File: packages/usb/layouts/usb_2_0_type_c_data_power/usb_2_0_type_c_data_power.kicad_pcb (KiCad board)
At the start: 2 copper layers, 5 parts

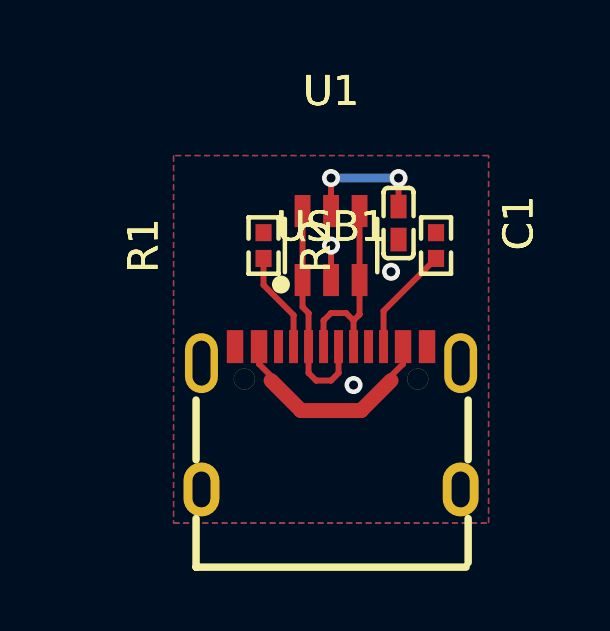
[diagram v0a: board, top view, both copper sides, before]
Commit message: Add ESP32S3, BM9002, Logic; Various naming updates and splitting of packages
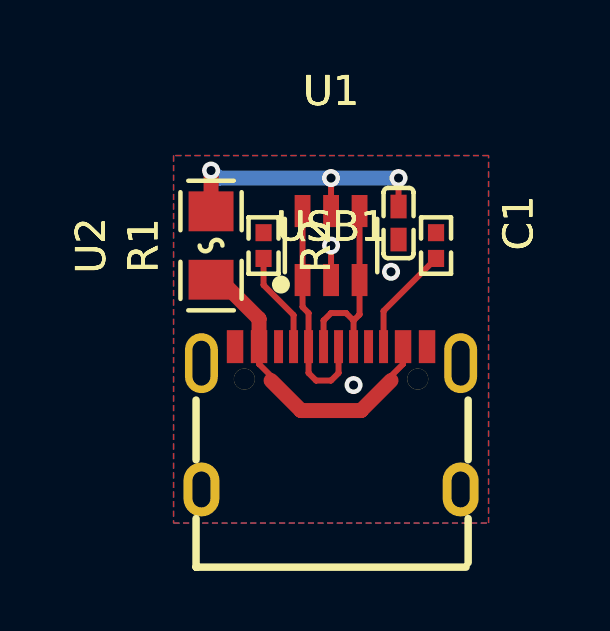
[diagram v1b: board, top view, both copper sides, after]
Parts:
- added U2: , atopile:F0805-d5954a, F.Cu at (-4.00, -5.75)
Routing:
- net hv: track 4.30 -> 9.76 mm, vias 2 -> 3
- net VBUS: track 7.42 -> 10.5 mm

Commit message: Build all packages without designators on silkscreen.
Also disable fail_on_drc and enable keep_picked_parts for build
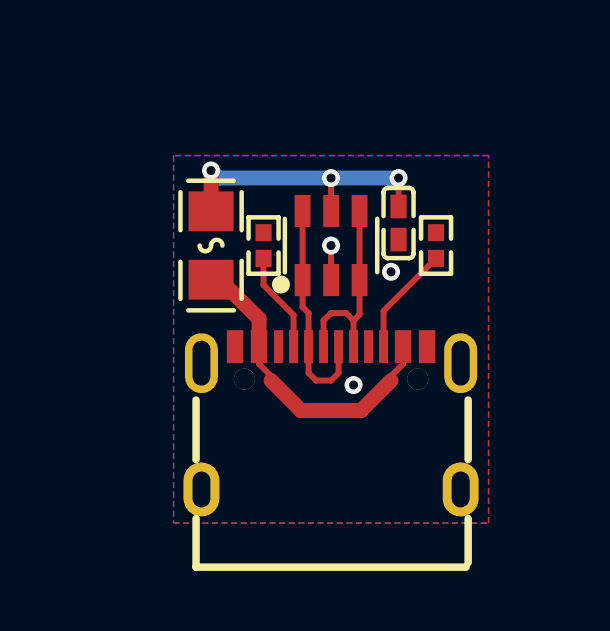
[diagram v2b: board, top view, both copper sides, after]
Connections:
- U1 pad 1: line-1 -> line
- U1 pad 3: line -> line-1
- U1 pad 4: line -> line-1
- U1 pad 6: line-1 -> line
- USB1 pad 5: line-1 -> line
- USB1 pad 6: line -> line-1
- USB1 pad 7: line-1 -> line
- USB1 pad 8: line -> line-1
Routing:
- net line-1: track 7.57 -> 6.68 mm
- net line: track 6.68 -> 7.57 mm

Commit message: Add USB PD trigger
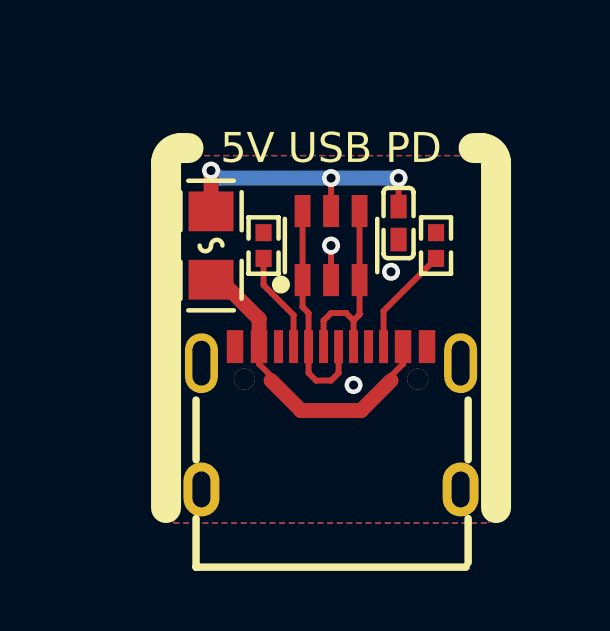
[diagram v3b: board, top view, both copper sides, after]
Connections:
- U1 pad 1: line -> line-1
- U1 pad 3: line-1 -> line
- U1 pad 4: line-1 -> line
- U1 pad 6: line -> line-1
- USB1 pad 5: line -> line-1
- USB1 pad 6: line-1 -> line
- USB1 pad 7: line -> line-1
- USB1 pad 8: line-1 -> line
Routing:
- net line-1: track 6.68 -> 7.57 mm
- net line: track 7.57 -> 6.68 mm
- net gnd: vias 3 -> 2
- net (no net): vias 0 -> 1
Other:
- board text added: "5V USB PD"

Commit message: Rebuild all
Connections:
- U1 pad 1: line-1 -> line
- U1 pad 3: line -> line-1
- U1 pad 4: line -> line-1
- U1 pad 6: line-1 -> line
- USB1 pad 5: line-1 -> line
- USB1 pad 6: line -> line-1
- USB1 pad 7: line-1 -> line
- USB1 pad 8: line -> line-1
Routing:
- net line-1: track 7.57 -> 6.68 mm
- net line: track 6.68 -> 7.57 mm
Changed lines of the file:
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@@
     (net 1 "SBU1")
     (net 2 "SBU2")
-    (net 3 "line-1")
-    (net 4 "line")
+    (net 3 "line")
+    (net 4 "line-1")
     (net 5 "hv")
     (net 6 "VBUS")
@@
             (size 0.53 1.07)
             (layers "F.Cu" "F.Mask" "F.Paste")
-            (net 3 "line-1")
+            (net 3 "line")
         )
         (pad "2" smd rect
@@
             (size 0.53 1.07)
             (layers "F.Cu" "F.Mask" "F.Paste")
-            (net 4 "line")
+            (net 4 "line-1")
         )
         (pad "4" smd rect
@@
             (size 0.53 1.07)
             (layers "F.Cu" "F.Mask" "F.Paste")
-            (net 4 "line")
+            (net 4 "line-1")
         )
         (pad "5" smd rect
@@
             (size 0.53 1.07)
             (layers "F.Cu" "F.Mask" "F.Paste")
-            (net 3 "line-1")
+            (net 3 "line")
         )
         (embedded_fonts no)
@@
             (size 0.3 1.1)
             (layers "F.Cu" "F.Mask" "F.Paste")
-            (net 3 "line-1")
+            (net 3 "line")
         )
         (pad "6" smd rect
@@
             (size 0.3 1.1)
             (layers "F.Cu" "F.Mask" "F.Paste")
-            (net 4 "line")
+            (net 4 "line-1")
         )
         (pad "7" smd rect
@@
             (size 0.3 1.1)
             (layers "F.Cu" "F.Mask" "F.Paste")
-            (net 3 "line-1")
+            (net 3 "line")
         )
         (pad "8" smd rect
@@
             (size 0.3 1.1)
             (layers "F.Cu" "F.Mask" "F.Paste")
-            (net 4 "line")
+            (net 4 "line-1")
         )
         (pad "9" smd rect
